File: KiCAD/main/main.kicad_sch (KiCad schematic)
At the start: 42 parts, among them J1 USB_C_Receptacle_USB2.0_14P, J2 Conn_Coaxial, SW1 SW_SPDT, SW2 SW_Push, SW3 SW_Push, U1 SX1262IMLTRT, U2 TP4056-42-ESOP8, U3 TLV75533PDRV, U4 ESP32-S3-MINI-1, U5 BGS12WN6E6327

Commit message: started repo and creation
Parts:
- removed C5, C8: 10uF, Capacitor_SMD:C_01005_0402Metric, symbol Device:C
- removed C9: 0.1uF, Capacitor_SMD:C_01005_0402Metric, symbol Device:C
- added C17, C18: 0.1uF, Capacitor_SMD:C_01005_0402Metric, symbol Device:C
- added D5: LED, LED_SMD:LED_0402_1005Metric, symbol Device:LED
- added R12: 1K, Resistor_SMD:R_01005_0402Metric, symbol Device:R
- added U7: CH340X, Package_SO:MSOP-10_3x3mm_P0.5mm, symbol Interface_USB:CH340X
- BT1: footprint Battery:BatteryHolder_MPD_BK-18650-PC2 -> Connector_JST:JST_PH_S2B-PH-K_1x02_P2.00mm_Horizontal
- C14: value 100nF -> 10uF
- R1, R2: footprint (none) -> Resistor_SMD:R_01005_0402Metric
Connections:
- net GND: now also C14.1, C17.1, C18.1, U7.3 (GND); no longer C14.2
- net USB_DATA+: now also U7.1 (UD+)
- net USB_DATA-: now also U7.2 (UD-)
- net V+: now also U2.8 (CE)
- net VCC: now also C14.2, C17.2, C18.2, U7.10 (V3), U7.7 (VCC); no longer C14.1
- net at U4.31 (IO35): now also R12.1
- net at U4.32 (IO36): now also D5.1 (K)
- net SERIAL_N: now reaches U4.39 (TXD0)
- net SERIAL_N: now also U7.9 (RXD)
- net SERIAL_P: now reaches U4.40 (RXD0)
- net SERIAL_P: now also U7.8 (TXD)
- net at D1.1 (K), D2.1 (K), SW1.2 (B): no longer C1.2, U3.6 (IN)
- net at SW1.1 (A), U3.4 (EN): now also C1.2, U3.6 (IN)
- net STCHR: no longer names the net of U4.8 (IO4)
- net STCHR: no longer U2.8 (CE)
- new net: D5.2 (A), R12.2
- no-connect marks 5 -> 10
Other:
- moved on the sheet: BT1, C1, C10, C11, C12, C13, C15, C16, C2, C3, C4, C6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

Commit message: rev 2!
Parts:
- removed D3, D4, D5: LED, LED_SMD:LED_0402_1005Metric, symbol Device:LED
- removed FL1: 0900FM15K0039001E, customlib:0900FM15K0039001E_JOT-L, symbol 2026-07-02_21-18-09:0900FM15K0039001E
- removed R12: 1K, Resistor_SMD:R_01005_0402Metric, symbol Device:R
- removed R3, R8: 10K, Resistor_SMD:R_01005_0402Metric, symbol Device:R
- removed R6: 2K, Resistor_SMD:R_01005_0402Metric, symbol Device:R
- removed SW2: SW_Push, Button_Switch_SMD:SW_SPST_PTS810, symbol Switch:SW_Push
- removed SW3: SW_Push, Button_Switch_SMD:SW_SPST_PTS645Sx43SMTR92, symbol Switch:SW_Push
- removed U3: TLV75533PDRV, Package_SON:WSON-6-1EP_2x2mm_P0.65mm_EP1x1.6mm, symbol Regulator_Linear:TLV75533PDRV
- removed U5: BGS12WN6E6327, Package_LGA:Infineon_PG-TSNP-6-10_0.7x1.1mm_0.7x1.1mm_P0.4mm, symbol RF_Switch:BGS12WN6E6327
- added C5: 470pF, Capacitor_SMD:C_0603_1608Metric, symbol Device:C
- added FL1: 0900FM15K0039, RF_Converter:Balun_Johanson_0900FM15K0039, symbol Filter:0900FM15K0039
- added R10, R9: 10K, Resistor_SMD:R_0603_1608Metric, symbol Device:R
- added U3: BGS12P2L, Package_LGA:Infineon_PG-TSNP-6-10_0.7x1.1mm_0.7x1.1mm_P0.4mm, symbol Personal:BGS12P2L
- added U6: MIC5219-3.3YMM, Package_SO:MSOP-8_3x3mm_P0.65mm, symbol Regulator_Linear:MIC5219-3.3YMM
- BT1: LCSC Part # (none) -> C265094
- C1, C2: footprint Capacitor_SMD:C_01005_0402Metric -> Capacitor_SMD:C_0603_1608Metric; LCSC Part # (none) -> C15849
- C10, C11, C13, C3, C6, C7: footprint Capacitor_SMD:C_01005_0402Metric -> Capacitor_SMD:C_0402_1005Metric; LCSC Part # (none) -> C1525
- C12: footprint Capacitor_SMD:C_01005_0402Metric -> Capacitor_SMD:C_0603_1608Metric; LCSC Part # (none) -> C1653
- C14, C15, C16: footprint Capacitor_SMD:C_01005_0402Metric -> Capacitor_SMD:C_0603_1608Metric; LCSC Part # (none) -> C19702
- C17, C18: footprint Capacitor_SMD:C_01005_0402Metric -> Capacitor_SMD:C_0402_1005Metric
- C4: footprint Capacitor_SMD:C_01005_0402Metric -> Capacitor_SMD:C_0805_2012Metric; LCSC Part # (none) -> C45783
- D1, D2: footprint Diode_SMD:D_01005_0402Metric -> Diode_SMD:D_SOD-323; LCSC Part # (none) -> C191023
- J1: LCSC Part # (none) -> C2765186
- J2: LCSC Part # (none) -> C3039673
- L1: footprint Inductor_SMD:L_01005_0402Metric -> Inductor_SMD:L_0805_2012Metric; LCSC Part # (none) -> C383402
- L2: footprint Inductor_SMD:L_01005_0402Metric -> Inductor_SMD:L_0603_1608Metric; LCSC Part # (none) -> C19721138
- R1, R2: footprint Resistor_SMD:R_01005_0402Metric -> Resistor_SMD:R_0603_1608Metric; LCSC Part # (none) -> C23186
- R4: footprint Resistor_SMD:R_01005_0402Metric -> Resistor_SMD:R_0603_1608Metric; LCSC Part # (none) -> C25804
- R5: footprint Resistor_SMD:R_01005_0402Metric -> Resistor_SMD:R_0402_1005Metric; LCSC Part # (none) -> C25076
- R7: footprint Resistor_SMD:R_01005_0402Metric -> Resistor_SMD:R_0603_1608Metric; LCSC Part # (none) -> C22765
- SW1: footprint Button_Switch_SMD:SW_SPDT_PCM12 -> customlib:SSSS810701; LCSC Part # (none) -> C97433
- U1: LCSC Part # (none) -> C191341
- U2: LCSC Part # (none) -> C16581
- U4: now left out of the parts list
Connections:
- net GND: now also C5.2, FL1.10 (GND), FL1.2 (GND), FL1.5 (GND), FL1.7 (GND), FL1.9 (GND), U3.2 (GND), U6.5 (GND), U6.6 (GND), U6.7 (GND), U6.8 (GND)
- net READY: now also U4.11 (IO7); no longer U4.13 (IO9)
- net SPI_CLK: now also U4.8 (IO4); no longer U4.10 (IO6)
- net SPI_CS: now also U4.7 (IO3); no longer U4.9 (IO5)
- net SPI_MISO: now also U4.9 (IO5); no longer U4.12 (IO8)
- net SPI_MOSI: now also U4.10 (IO6); no longer U4.11 (IO7)
- net VCC: now also R10.2, R9.2, U3.4 (VDD), U6.3 (OUT)
- net at J2.1 (In): now also U3.5 (RFIN)
- net at U1.21 (RFI_P): now also FL1.4 (RFI_P)
- net at U1.22 (RFI_N): now also FL1.3 (RFI_N)
- net at L2.2, U1.23 (RFO): now also FL1.1 (RFO)
- net ~{CHRG}: now reaches U4.20 (IO16)
- net ~{CHRG}: now also U2.7 (~{CHRG}), R10.1
- net ~{STDBY}: now reaches U4.21 (IO17)
- net ~{STDBY}: now also U2.6 (~{STDBY}), R9.1
- net TDI: now reaches U4.35 (IO39)
- net TDO: now reaches U4.36 (IO40)
- net TCK: now reaches U4.37 (IO41)
- net TMS: now reaches U4.38 (IO42)
- net at C1.2, SW1.1 (A): now also U6.1 (EN), U6.2 (IN)
- net at C13.1, R5.2: now also U3.6 (CTRL)
- net CHRG renamed CHRG_BAT
- new net: FL1.8 (SW_RFO), U3.1 (RF2)
- new net: FL1.6 (SW_RFI), U3.3 (RF1)
- new net: C5.1, U6.4 (BP)
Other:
- note added: "NOTE 2: Ensure a solid, continuous ground plane directly beneath the entire RF path and the filter."
- note removed: "NOTE 2: Ensure a solid, continuous ground plane directly beneath the entire RF path and the Johanson filter."
- moved on the sheet: C10, C13, C15, C16, C17, C18, C2, J1, J2, R1, R2, R5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

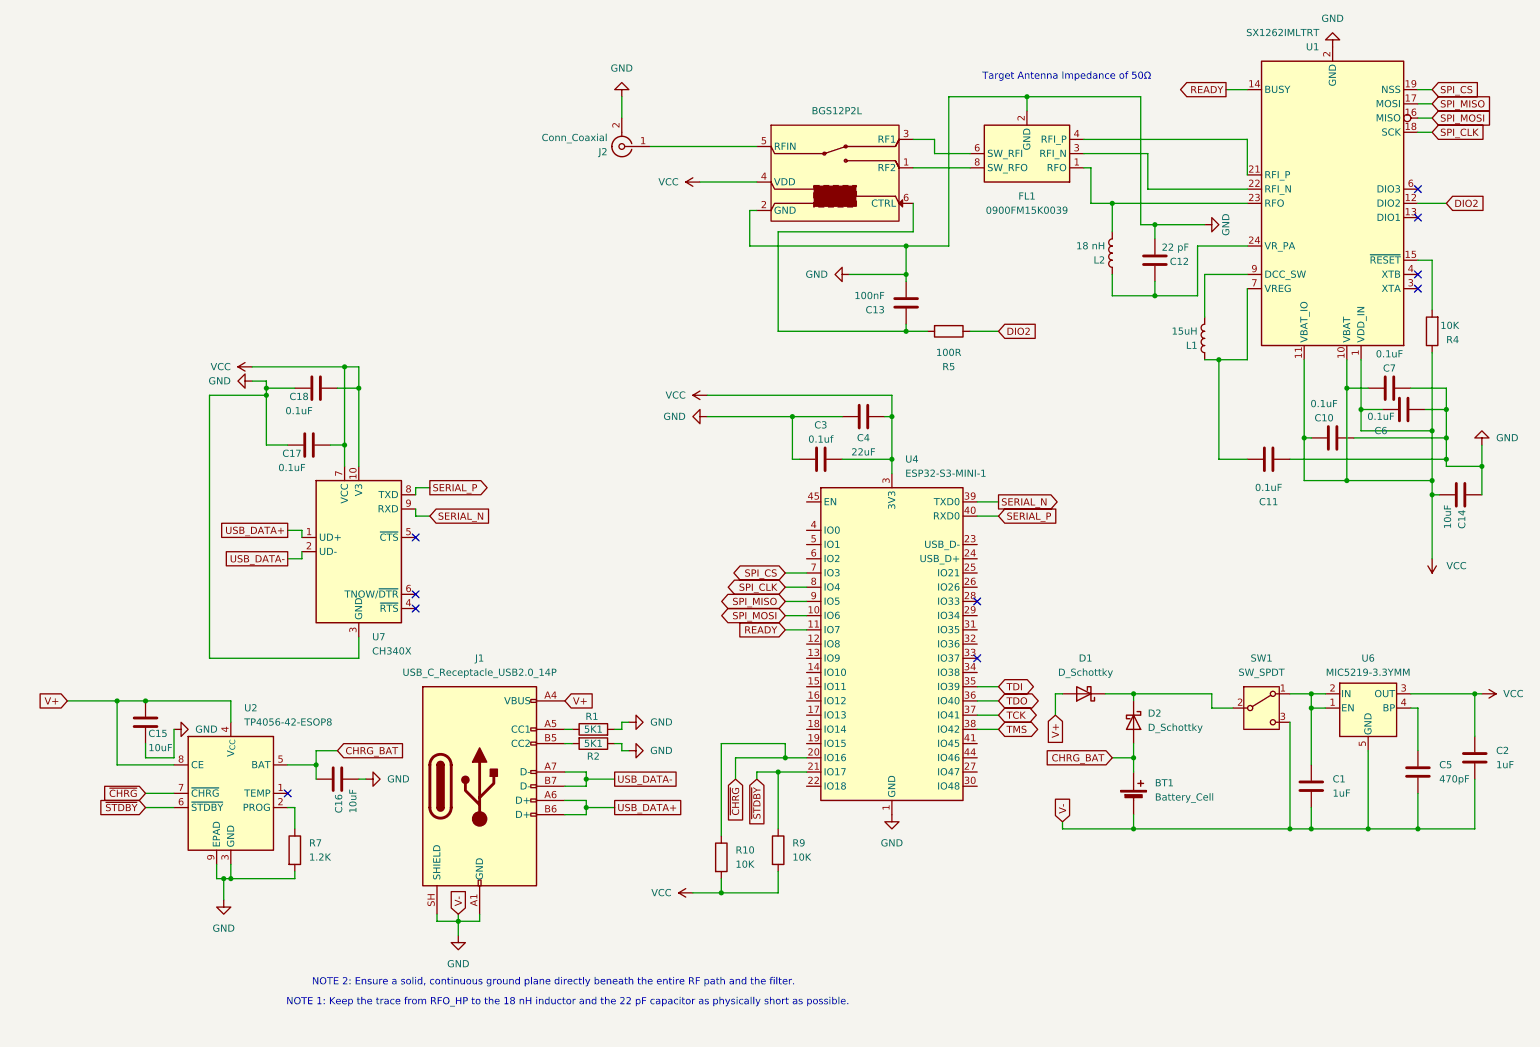
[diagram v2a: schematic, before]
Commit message: added screen to rev 2 and bumped version to 2.1
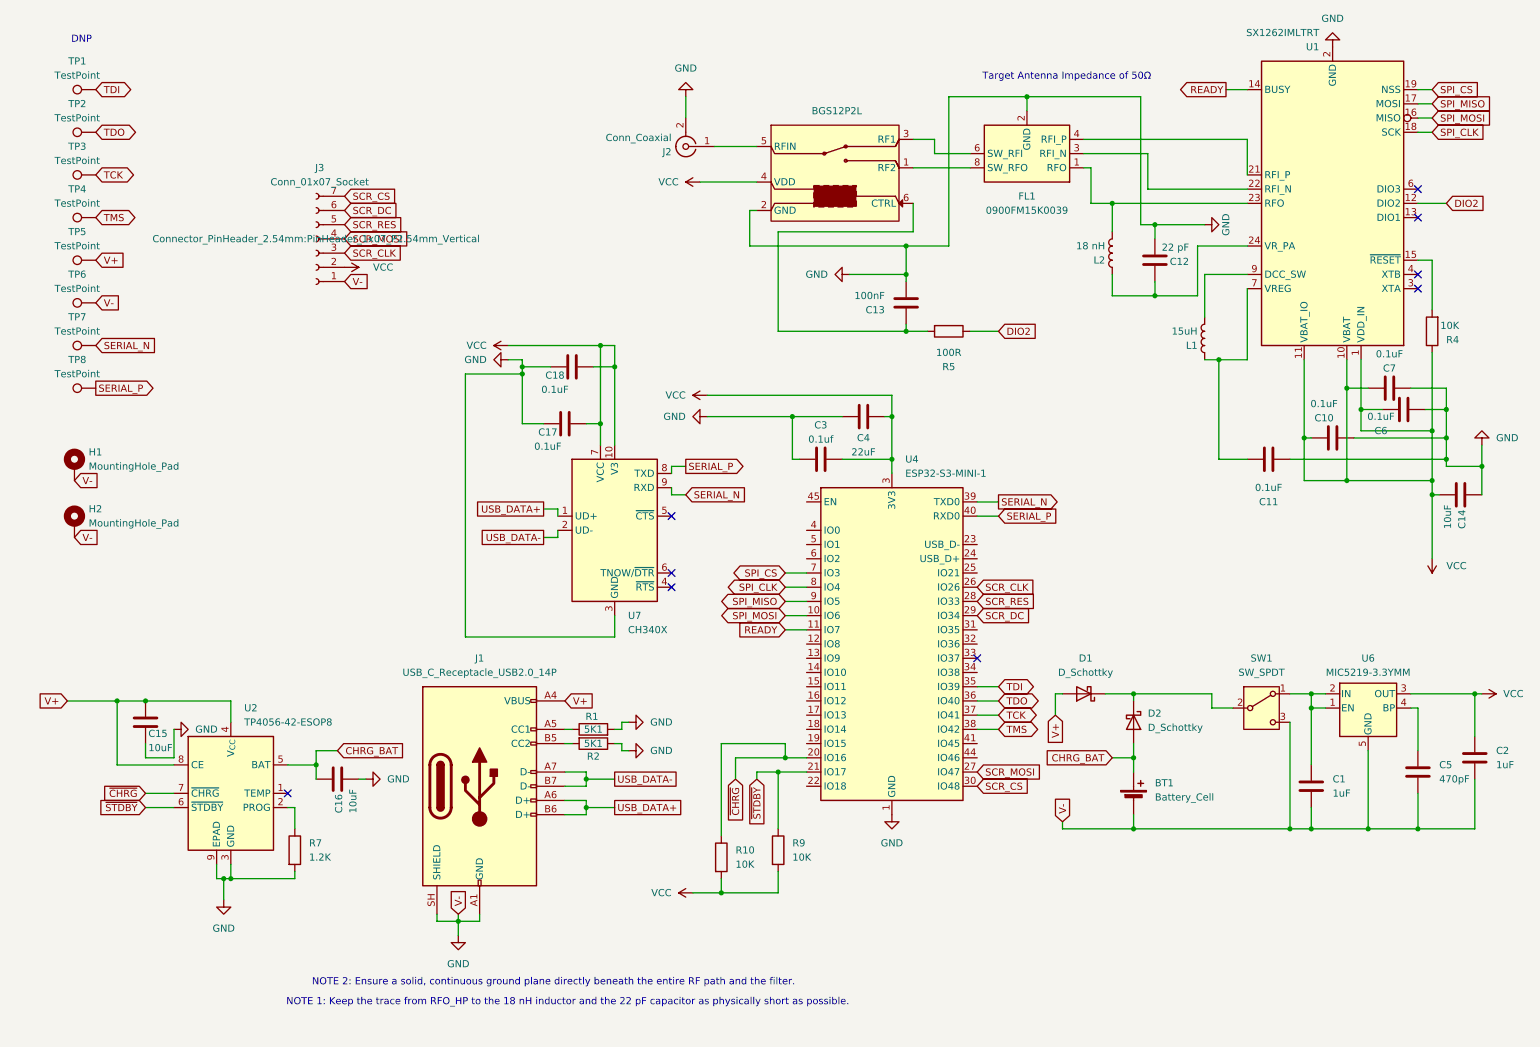
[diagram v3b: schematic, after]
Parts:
- added H1, H2: MountingHole_Pad, MountingHole:MountingHole_2.2mm_M2_DIN965_Pad_TopBottom, symbol Mechanical:MountingHole_Pad
- added J3: Conn_01x07_Socket, Connector_PinHeader_2.54mm:PinHeader_1x07_P2.54mm_Vertical, symbol Connector:Conn_01x07_Socket
- added TP1, TP2, TP3, TP4, TP5, TP6, TP7, TP8: TestPoint, TestPoint:TestPoint_Pad_1.5x1.5mm, symbol Connector:TestPoint
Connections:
- net GND: now also H1.1, H2.1, J3.1 (Pin_1), TP6.1
- net SERIAL_N: now also TP7.1
- net SERIAL_P: now also TP8.1
- net TCK: now also TP3.1
- net TDI: now also TP1.1
- net TDO: now also TP2.1
- net TMS: now also TP4.1
- net V+: now also TP5.1
- net VCC: now also J3.2 (Pin_2)
- net SCR_CLK: now reaches U4.26 (IO26)
- net SCR_CLK: now also J3.3 (Pin_3)
- net SCR_MOSI: now reaches U4.27 (IO47)
- net SCR_MOSI: now also J3.4 (Pin_4)
- net SCR_RES: now reaches U4.28 (IO33)
- net SCR_RES: now also J3.5 (Pin_5)
- net SCR_DC: now reaches U4.29 (IO34)
- net SCR_DC: now also J3.6 (Pin_6)
- net SCR_CS: now reaches U4.30 (IO48)
- net SCR_CS: now also J3.7 (Pin_7)
- no-connect marks 10 -> 9
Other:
- note added: "DNP"
- moved on the sheet: C17, C18, J2, U7
